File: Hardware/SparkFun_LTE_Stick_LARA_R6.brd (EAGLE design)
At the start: 25.4 x 82.5 mm, 130 parts, among them IC1 SN74AVC4T774PW, IC3 SN74AVC4T774PW, J1 NANO_SIM, U1 LARA-R6401, U2 AP7361C-33

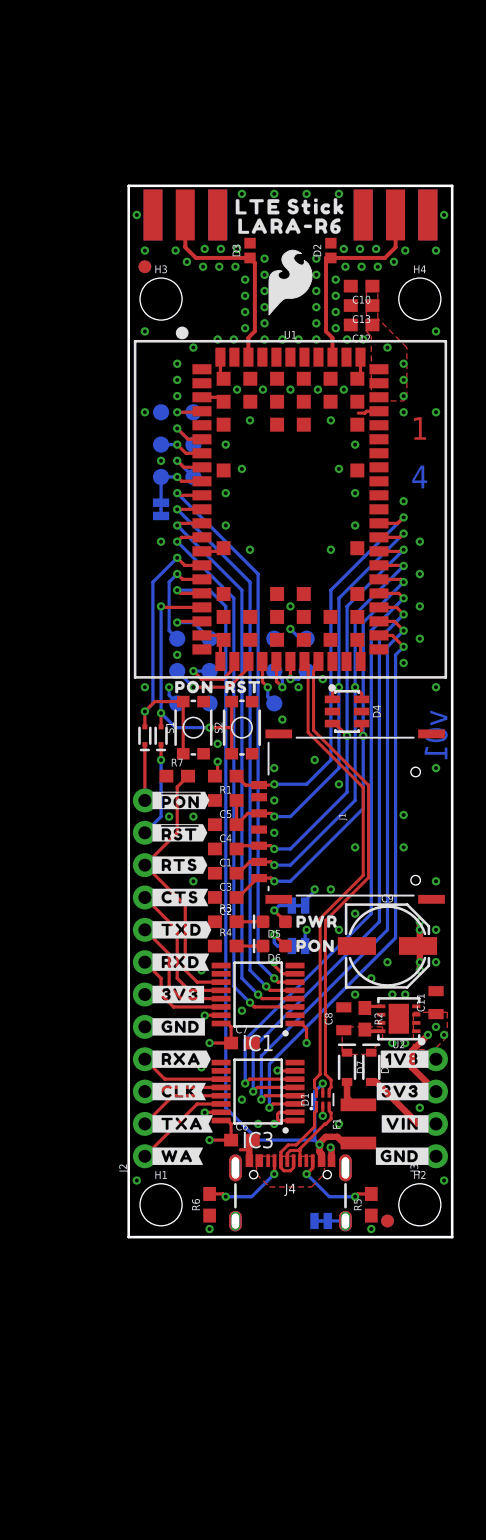
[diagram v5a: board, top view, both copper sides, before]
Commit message: Design review updates
Update Eagle libraries to fix vector fonts for some symbols
Add GND vias near SIM holder pads
Add max input voltage for VREG
Straighten USB trace near connector (N$10)
Fix trace on ANT1 ESD pad
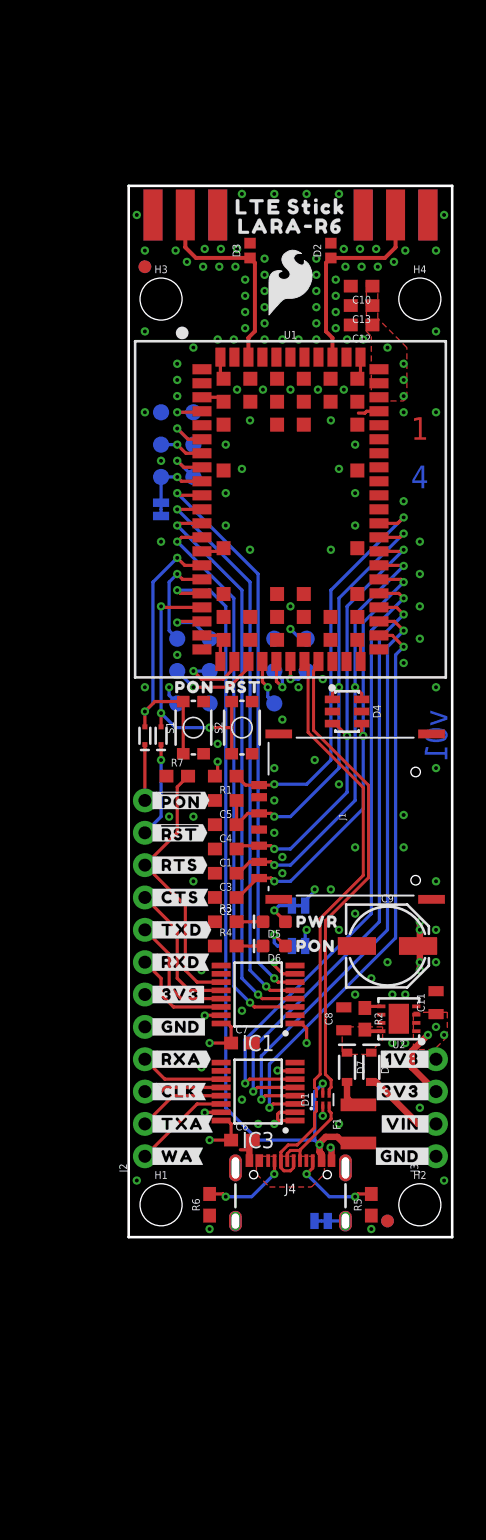
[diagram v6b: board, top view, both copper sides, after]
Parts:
- D2, D3: value PESD0402 -> PESD0402-0402
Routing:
- net GND: vias 130 -> 132
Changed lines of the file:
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@@
 <wire x1="6.985" y1="5.08" x2="5.715" y2="5.08" width="0.254" layer="22"/>
 <rectangle x1="7.112" y1="23.622" x2="7.239" y2="24.003" layer="41"/>
-<rectangle x1="11.303" y1="28.448" x2="11.43" y2="28.702" layer="42"/>
-<rectangle x1="11.303" y1="29.718" x2="11.43" y2="29.972" layer="42"/>
+<rectangle x1="12.7" y1="28.448" x2="12.827" y2="28.702" layer="42"/>
+<rectangle x1="12.7" y1="29.718" x2="12.827" y2="29.972" layer="42"/>
 <rectangle x1="13.97" y1="34.925" x2="14.097" y2="35.179" layer="42"/>
 <dimension x1="0" y1="0" x2="2.54" y2="0" x3="1.27" y3="-3.81" textsize="1.778" textratio="15" layer="47" unit="inch"/>
@@
 <attribute name="VALUE" x="10.16" y="22.86" size="1.27" layer="27" rot="R180" align="center"/>
 </element>
-<element name="D2" library="SparkFun-DiscreteSemi" package="0402" value="PESD0402" x="15.875" y="77.47" smashed="yes" rot="R90">
+<element name="D2" library="SparkFun-DiscreteSemi" package="0402" value="PESD0402-0402" x="15.875" y="77.47" smashed="yes" rot="R90">
 <attribute name="DIGIKEY_PART" value="PESD0402-140CT-ND" x="15.875" y="76.2" size="1.778" layer="27" font="vector" ratio="15" rot="R90" display="off"/>
 <attribute name="MOUSE_PART" value="650-PESD0402-140" x="15.875" y="76.2" size="1.778" layer="27" font="vector" ratio="15" rot="R90" display="off"/>
@@
 <attribute name="VALUE" x="16.637" y="77.47" size="0.6096" layer="27" font="vector" ratio="20" rot="R90" align="top-center"/>
 </element>
-<element name="D3" library="SparkFun-DiscreteSemi" package="0402" value="PESD0402" x="9.525" y="77.47" smashed="yes" rot="R90">
+<element name="D3" library="SparkFun-DiscreteSemi" package="0402" value="PESD0402-0402" x="9.525" y="77.47" smashed="yes" rot="R90">
 <attribute name="DIGIKEY_PART" value="PESD0402-140CT-ND" x="9.525" y="76.2" size="1.778" layer="27" font="vector" ratio="15" rot="R90" display="off"/>
 <attribute name="MOUSE_PART" value="650-PESD0402-140" x="9.525" y="76.2" size="1.778" layer="27" font="vector" ratio="15" rot="R90" display="off"/>
@@
 <via x="20.32" y="21.59" extent="1-16" drill="0.3048"/>
 <via x="15.875" y="27.305" extent="1-16" drill="0.3048"/>
+<via x="12.065" y="28.575" extent="1-16" drill="0.3048"/>
+<via x="12.065" y="29.845" extent="1-16" drill="0.3048"/>
 </signal>
 <signal name="3.3V">
@@
 <wire x1="20.955" y1="77.724" x2="20.955" y2="80.264" width="0.31241875" layer="1"/>
 <wire x1="20.121" y1="76.89" x2="20.955" y2="77.724" width="0.31241875" layer="1"/>
-<wire x1="15.494" y1="76.89" x2="15.875" y2="76.89" width="0.31241875" layer="1"/>
-<wire x1="15.494" y1="71.12" x2="15.494" y2="76.89" width="0.31241875" layer="1"/>
+<wire x1="15.494" y1="76.509" x2="15.875" y2="76.89" width="0.31241875" layer="1"/>
+<wire x1="15.494" y1="71.12" x2="15.494" y2="76.509" width="0.31241875" layer="1"/>
 </signal>
 <signal name="ANT2" class="2">
@@
 <wire x1="15.74" y1="9.9078" x2="15.74" y2="10.365" width="0.23926875" layer="1"/>
 <wire x1="15.8924" y1="9.7554" x2="15.8924" y2="9.2884" width="0.23926875" layer="1"/>
-<wire x1="15.4813" y1="8.8773" x2="15.8924" y2="9.2884" width="0.23926875" layer="1"/>
-<wire x1="13.45" y1="6.9342" x2="15.3931" y2="8.8773" width="0.23926875" layer="1"/>
-<wire x1="15.3931" y1="8.8773" x2="15.4813" y2="8.8773" width="0.23926875" layer="1"/>
-<wire x1="13.45" y1="6.9342" x2="13.45" y2="6.8072" width="0.23926875" layer="1"/>
+<wire x1="13.45" y1="6.846" x2="15.8924" y2="9.2884" width="0.23926875" layer="1"/>
+<wire x1="13.45" y1="6.846" x2="13.45" y2="6.8072" width="0.23926875" layer="1"/>
 </signal>
 <signal name="N$11">
@@
 <wire x1="14.74" y1="10.39" x2="14.74" y2="9.9074" width="0.23926875" layer="1"/>
 <wire x1="14.74" y1="9.9074" x2="14.5876" y2="9.755" width="0.23926875" layer="1"/>
-<wire x1="14.5876" y1="9.755" x2="14.5876" y2="8.6694" width="0.23926875" layer="1"/>
+<wire x1="14.5876" y1="9.755" x2="14.5876" y2="8.5932" width="0.23926875" layer="1"/>
 <wire x1="11.95" y1="6.6668" x2="11.95" y2="6.01" width="0.23926875" layer="1"/>
-<wire x1="14.5876" y1="8.6694" x2="13.1572" y2="7.239" width="0.23926875" layer="1"/>
-<wire x1="13.1572" y1="7.239" x2="12.5222" y2="7.239" width="0.23926875" layer="1"/>
+<wire x1="14.5876" y1="8.5932" x2="13.2334" y2="7.239" width="0.23926875" layer="1"/>
+<wire x1="13.2334" y1="7.239" x2="12.5222" y2="7.239" width="0.23926875" layer="1"/>
 <wire x1="12.5222" y1="7.239" x2="11.95" y2="6.6668" width="0.23926875" layer="1"/>
 </signal>

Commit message: Clean up design
Increase frame to ledger size
Arrange test points in schematic to match physical layout
Add impedance calculations to schematic
Update LED VALUE attributes with color in schematic
Add silkscreen labels to test points
Decrease font size of top buzzard labels to make tails more visible
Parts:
- added U$56: (no value), output:UART20
- added U$57: (no value), output:GPIO0
- added U$58: (no value), output:I2C0
- D5, D6: value (none) -> Red
- FRAME1: value FRAME-LETTER -> FRAME-LEDGER
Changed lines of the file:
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@@
 <drawing>
 <settings>
-<setting alwaysvectorfont="yes"/>
+<setting alwaysvectorfont="no"/>
 <setting verticaltext="up"/>
 </settings>
@@
 Silkscreen: White
 Surface Finish: Lead-Free HASL</text>
+<wire x1="7.62" y1="42.545" x2="7.62" y2="41.275" width="0.2032" layer="22"/>
+<wire x1="10.16" y1="47.625" x2="10.16" y2="46.355" width="0.2032" layer="22"/>
+<wire x1="1.27" y1="65.405" x2="1.27" y2="64.135" width="0.2032" layer="22"/>
+<wire x1="12.7" y1="40.64" x2="12.7" y2="41.91" width="0.2032" layer="22"/>
+<wire x1="12.7" y1="41.91" x2="12.7" y2="46.99" width="0.2032" layer="22"/>
+<wire x1="5.08" y1="40.64" x2="5.08" y2="46.99" width="0.2032" layer="22"/>
+<wire x1="3.81" y1="66.04" x2="3.81" y2="59.69" width="0.2032" layer="22"/>
+<wire x1="3.175" y1="64.77" x2="4.445" y2="64.77" width="0.2032" layer="22"/>
+<wire x1="3.175" y1="62.23" x2="4.445" y2="62.23" width="0.2032" layer="22"/>
+<wire x1="3.175" y1="59.69" x2="4.445" y2="59.69" width="0.2032" layer="22"/>
+<wire x1="4.445" y1="46.99" x2="5.715" y2="46.99" width="0.2032" layer="22"/>
+<wire x1="4.445" y1="44.45" x2="5.715" y2="44.45" width="0.2032" layer="22"/>
+<wire x1="4.445" y1="41.91" x2="5.715" y2="41.91" width="0.2032" layer="22"/>
+<wire x1="12.065" y1="46.99" x2="13.335" y2="46.99" width="0.2032" layer="22"/>
+<wire x1="12.065" y1="44.45" x2="13.335" y2="44.45" width="0.2032" layer="22"/>
+<wire x1="12.7" y1="41.91" x2="12.065" y2="41.91" width="0.2032" layer="22"/>
 </plain>
 <attributes>
@@
 </class>
 <class number="2" name="RF" width="0.31241875" drill="0">
+<clearance class="0" value="0.1778"/>
 </class>
 </classes>
@@
 <attribute name="VALUE" x="22.86" y="71.628" size="0.6096" layer="27" font="vector" ratio="20" align="top-center"/>
 </element>
-<element name="FRAME1" library="SparkFun-Aesthetics" package="CREATIVE_COMMONS" value="FRAME-LETTER" x="-10.16" y="-25.4" smashed="yes">
-<attribute name="DESIGNER" value="Dryw Wade" x="-10.16" y="-25.4" size="1.778" layer="27" font="vector" ratio="15" display="off"/>
-<attribute name="REV" value="v01" x="-10.16" y="-25.4" size="1.778" layer="27" font="vector" ratio="15" display="off"/>
-</element>
 <element name="U1" library="SparkFun-RF" package="LARA-LGA" value="LARA-R6401" x="12.7" y="57.15" smashed="yes" rot="R270">
 <attribute name="NAME" x="12.7" y="70.55" size="0.6096" layer="25" font="vector" ratio="20" align="bottom-center"/>
@@
 <element name="U$10" library="output" package="#DTR#0" value="" x="3.175" y="57.15" smashed="yes" rot="MR0"/>
 <element name="LOGO2" library="SparkFun-Aesthetics" package="OSHW-LOGO-M" value="OSHW-LOGOM" x="12.7" y="79.375" smashed="yes" rot="MR0"/>
-<element name="D5" library="SparkFun-LED" package="LED-0603" value="" x="11.43" y="24.765" smashed="yes" rot="R180">
+<element name="D5" library="SparkFun-LED" package="LED-0603" value="Red" x="11.43" y="24.765" smashed="yes" rot="R180">
 <attribute name="NAME" x="11.43" y="24.13" size="0.6096" layer="25" font="vector" ratio="20" rot="R180" align="bottom-center"/>
 <attribute name="PROD_ID" value="DIO-17976" x="11.43" y="24.765" size="1.778" layer="27" rot="R180" display="off"/>
-<attribute name="VALUE" x="11.43" y="25.4" size="0.6096" layer="27" font="vector" ratio="20" rot="R180" align="top-center"/>
-</element>
-<element name="D6" library="SparkFun-LED" package="LED-0603" value="" x="11.43" y="22.86" smashed="yes" rot="R180">
+<attribute name="VALUE" value="Red" x="11.43" y="25.4" size="0.6096" layer="27" font="vector" ratio="20" rot="R180" align="top-center"/>
+</element>
+<element name="D6" library="SparkFun-LED" package="LED-0603" value="Red" x="11.43" y="22.86" smashed="yes" rot="R180">
 <attribute name="NAME" x="11.43" y="22.225" size="0.6096" layer="25" font="vector" ratio="20" rot="R180" align="bottom-center"/>
 <attribute name="PROD_ID" value="DIO-17976" x="11.43" y="22.86" size="1.778" layer="27" rot="R180" display="off"/>
-<attribute name="VALUE" x="11.43" y="23.495" size="0.6096" layer="27" font="vector" ratio="20" rot="R180" align="top-center"/>
+<attribute name="VALUE" value="Red" x="11.43" y="23.495" size="0.6096" layer="27" font="vector" ratio="20" rot="R180" align="top-center"/>
 </element>
 <element name="PWR" library="SparkFun-Jumpers" package="SMT-JUMPER_2_NC_TRACE_SILK" package3d_urn="urn:adsk.eagle:package:39281/1" value="JUMPER-SMT_2_NC_TRACE_SILK" x="13.335" y="26.035" smashed="yes" rot="MR180">
@@
 <element name="U$54" library="output" package="3#3V0" value="" x="7.62" y="49.53" smashed="yes" rot="MR0"/>
 <element name="U$55" library="SparkFun-Aesthetics" package="ORDERING_INSTRUCTIONS" value="" x="40.64" y="50.8" smashed="yes"/>
+<element name="FRAME1" library="SparkFun-Aesthetics" package="CREATIVE_COMMONS" value="FRAME-LEDGER" x="-10.16" y="-25.4" smashed="yes">
+<attribute name="DESIGNER" value="Dryw Wade" x="-10.16" y="-25.4" size="1.778" layer="27" display="off"/>
+<attribute name="REV" value="v01" x="-10.16" y="-25.4" size="1.778" layer="27" display="off"/>
+</element>
+<element name="U$56" library="output" package="UART20" value="" x="3.81" y="66.675" smashed="yes" rot="MR0"/>
+<element name="U$57" library="output" package="GPIO0" value="" x="5.08" y="40.005" smashed="yes" rot="MR0"/>
+<element name="U$58" library="output" package="I2C0" value="" x="12.7" y="40.005" smashed="yes" rot="MR0"/>
 </elements>
 <signals>

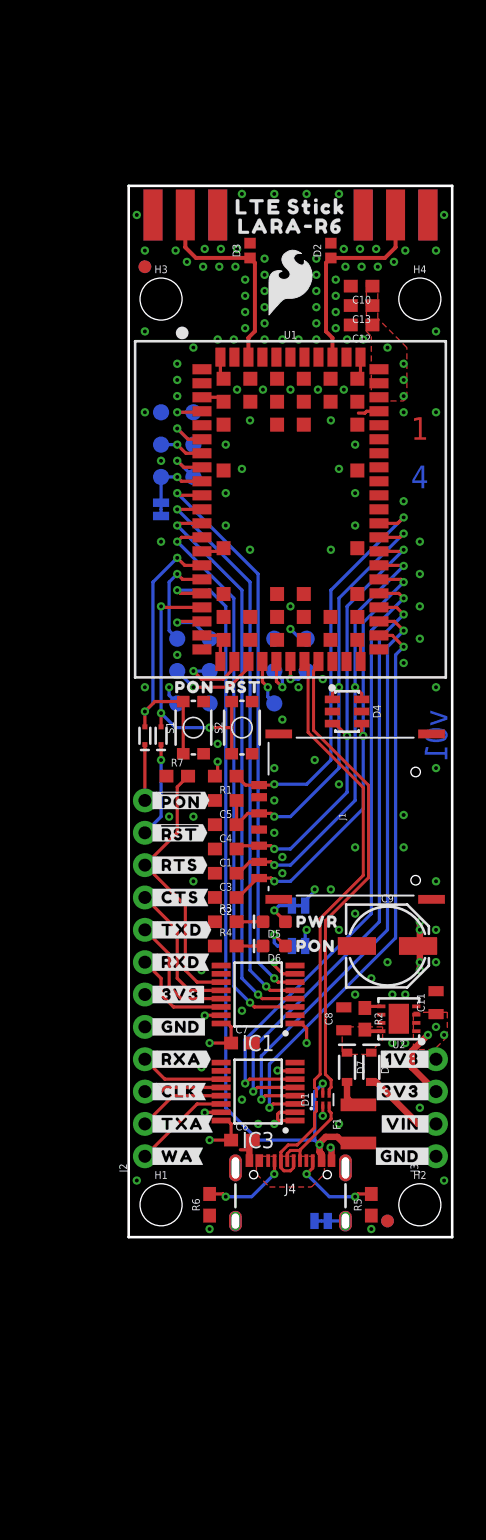
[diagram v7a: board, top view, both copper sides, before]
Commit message: v10 updates
Bump version number to v10
Add AT Commands Manual
Add Application Development App Note
Add Audio App Note
Fix text in Antenna Connectors section to be "Coplanar Waveguide Calculation"
Reposition D7 and D8 so text is horizontal
Change material to TG155 in ordering instructions
Nudge some vias to avoid silk
Shrink pin label size to 0.0375 so flags are visible
Replace PON with ON
Appaned "_LED" to LED jumpers
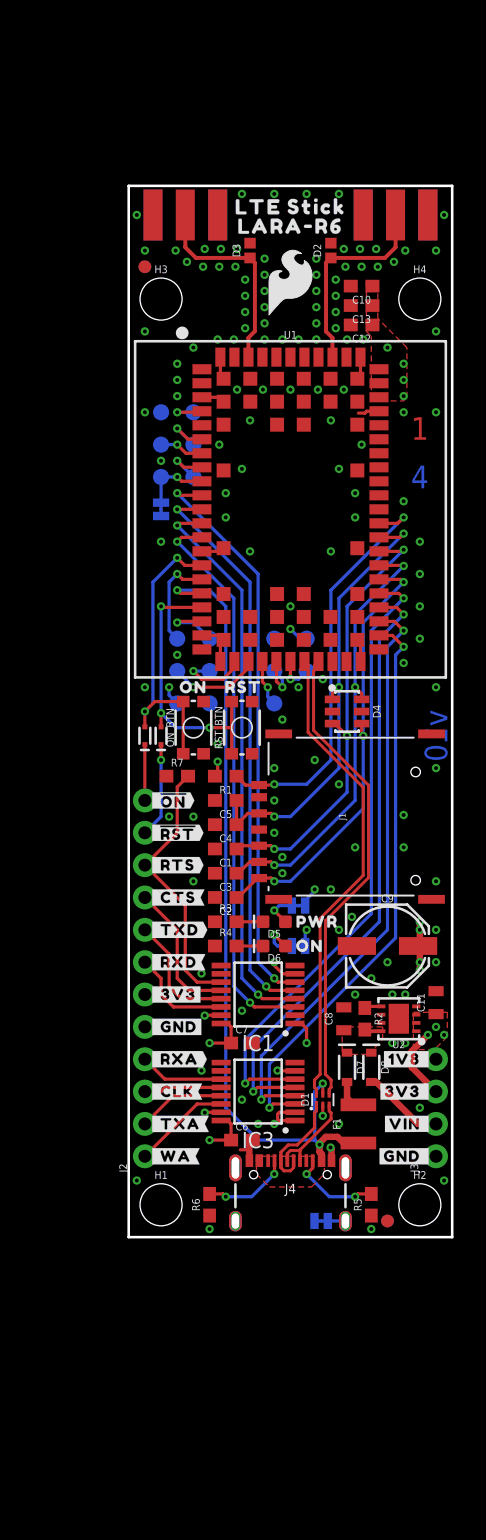
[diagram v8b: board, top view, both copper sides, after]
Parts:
- removed U$29: (no value), output:#_#PON##0
- removed U$36: (no value), output:#PWR#0
- added U$59: (no value), output:#_#ON##0
- added U$60: (no value), output:#PWR_LED#0
- U$37: device output:PON0 -> output:ON0
- U$39: device output:#PON#0 -> output:ON0
- U$53: device output:PON0 -> output:#ON_LED#0
- moved U$53 23.3 mm to (14.2, 22.9), flipped to the bottom
- moved U$37 22.3 mm to (3.30, 43.2)
- moved U$39 1.78 mm to (12.4, 22.9), flipped to the top
- renumbered PON to ON_LED, PWR to PWR_LED, S1 to ON_BTN, S2 to RST_BTN
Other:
- board text added: "4-layer JLC7628 Stackup Material: TG155 1oz outer layers 0.5oz inner layers Board thickness: 1.6mm Soldermask: Red Silkscreen: White Surface Finish: Lead-Free HASL"
- board text added: "v10"
- board text removed: "4-layer JLC7628 Stackup Material: TG135-140 1oz outer layers 0.5oz inner layers Board thickness: 1.6mm Soldermask: Red Silkscreen: White Surface Finish: Lead-Free HASL"
- board text removed: "v01"
